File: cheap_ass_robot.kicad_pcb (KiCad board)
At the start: 2 copper layers, 68.6 x 53.3 mm, 43 parts, among them IC1 MC34063A, IC2 ATMEGA328P-AU-R, IC3 FT232RL, IC4 L293DD, J1 USB_B, J2 DIGITAL 2, J3 ANALOG IN, J4 POWER, J5 DIGITAL 1, M1 Motor_DC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

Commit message: fixed diagram level electrical issues and added caps from xtal to gnd
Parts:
- added C6: 22pF, Capacitors_SMD:C_0805, F.Cu at (148.6, 69.8)
- added C7: 22pF, Capacitors_SMD:C_0805, F.Cu at (152.4, 69.8)
- renumbered C8 to C10, C9 to C11, C10 to C12, C11 to C13, C6 to C8, C7 to C9
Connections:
- C10 pad 1: Net-(C4-Pad1) -> Net-(C10-Pad1)
- C11 pad 1: Net-(C4-Pad1) -> Net-(C10-Pad1)
- C4 pad 1: Net-(C4-Pad1) -> Net-(C10-Pad1)
- C9 pad 1: Net-(C4-Pad1) -> Net-(C10-Pad1)
- D2 pad 1: Net-(C4-Pad1) -> Net-(C10-Pad1)
- D3 pad 1: Net-(C4-Pad1) -> Net-(C10-Pad1)
- D4 pad 2: Net-(C4-Pad1) -> Net-(C10-Pad1)
- D5 pad 2: Net-(C4-Pad1) -> Net-(C10-Pad1)
- IC2 pad 18: Net-(C4-Pad1) -> Net-(C10-Pad1)
- IC2 pad 21: Net-(IC2-Pad21) -> Net-(BT1-Pad2)
- IC2 pad 23: (no net) -> Net-(IC2-Pad23)
- IC2 pad 24: (no net) -> Net-(IC2-Pad24)
- IC2 pad 25: (no net) -> Net-(IC2-Pad25)
- IC2 pad 4: Net-(C4-Pad1) -> Net-(C10-Pad1)
- IC2 pad 6: Net-(C4-Pad1) -> Net-(C10-Pad1)
- IC3 pad 20: Net-(C4-Pad1) -> Net-(C10-Pad1)
- IC3 pad 4: Net-(C4-Pad1) -> Net-(C10-Pad1)
- IC4 pad 1: Net-(C4-Pad1) -> Net-(C10-Pad1)
- IC4 pad 10: Net-(C4-Pad1) -> Net-(C10-Pad1)
- IC4 pad 11: Net-(C4-Pad1) -> Net-(C10-Pad1)
- IC4 pad 14: Net-(IC4-Pad14) -> Net-(BT1-Pad2)
- IC4 pad 18: (no net) -> Net-(IC4-Pad18)
- IC4 pad 20: Net-(C4-Pad1) -> Net-(C10-Pad1)
- J2 pad 8: Net-(J2-Pad8) -> Net-(C10-Pad1)
- J3 pad 1: Net-(IC2-Pad20) -> Net-(IC2-Pad23)
- J3 pad 2: Net-(IC2-Pad21) -> Net-(IC2-Pad24)
- J3 pad 3: Net-(IC2-Pad22) -> Net-(IC2-Pad25)
- J4 pad 1: Net-(J2-Pad8) -> Net-(C10-Pad1)
- J4 pad 4: Net-(J2-Pad8) -> Net-(C10-Pad1)
- J4 pad 7: Net-(J2-Pad8) -> Net-(C10-Pad1)
- M2 pad 2: Net-(IC4-Pad14) -> Net-(IC4-Pad18)
- R4 pad 2: Net-(C4-Pad1) -> Net-(C10-Pad1)
- R6 pad 2: Net-(C4-Pad1) -> Net-(C10-Pad1)
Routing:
- net Net-(C4-Pad1): track 191.9 -> 0.00 mm, vias 15 -> 0
- net Net-(J2-Pad8): track 97.9 -> 0.00 mm
- net Net-(C10-Pad1): track 0.00 -> 40.8 mm, vias 0 -> 19
- net Net-(IC2-Pad25): track 0.00 -> 38.6 mm
- net Net-(IC2-Pad23): track 0.00 -> 36.7 mm
- net Net-(IC2-Pad24): track 0.00 -> 36.7 mm
- net Net-(IC2-Pad22): track 35.7 -> 0.00 mm
- net Net-(IC4-Pad14): track 34.7 -> 0.00 mm, vias 1 -> 0
- net Net-(IC2-Pad21): track 34.2 -> 0.00 mm
- net Net-(C3-Pad1): track 70.3 -> 44.3 mm, vias 8 -> 2
- net Net-(IC2-Pad31): track 38.5 -> 61.1 mm
- net Net-(IC4-Pad18): track 0.00 -> 22.0 mm, vias 0 -> 1
- net Net-(C6-Pad1): track 16.1 -> 33.0 mm
- net Net-(IC2-Pad30): track 41.7 -> 57.6 mm
- net Net-(IC2-Pad16): track 49.7 -> 38.2 mm, vias 2 -> 0
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- added copper zone on B.Cu, net Net-(C10-Pad1)

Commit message: will probably be revision alpha-1
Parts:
- added REF**: MountingHole_3.2mm_M3, Mounting_Holes:MountingHole_3.2mm_M3, F.Cu at (130.7, 63.1)
- added REF**: MountingHole_3.2mm_M3, Mounting_Holes:MountingHole_3.2mm_M3, F.Cu at (181.5, 78.4)
- added REF**: MountingHole_3.2mm_M3, Mounting_Holes:MountingHole_3.2mm_M3, F.Cu at (181.5, 106.3)
- added REF**: MountingHole_3.2mm_M3, Mounting_Holes:MountingHole_3.2mm_M3, F.Cu at (129.4, 111.3)
- C4: footprint Capacitors_SMD:CP_Elec_4x5.7 -> Capacitors_SMD:CP_Elec_6.3x7.7
- D2, D3: footprint Diodes_SMD:D_SMB -> Diodes_SMD:D_SOD-123F
- L1: footprint Inductors_SMD:L_1210 -> Inductors_SMD:L_0805
- moved C5 2.84 mm to (129.5, 85.1), turned to 180 degrees
- moved C7 2.54 mm to (154.9, 69.8), turned to 0 degrees
- moved C13 1.80 mm to (137.2, 85.1), turned to 180 degrees
- moved C6 1.27 mm to (149.9, 69.8), turned to 0 degrees
- moved D2 1.27 mm to (137.2, 106.7)
- moved C11 1.27 mm to (119.4, 63.5), turned to 180 degrees
- moved C9 1.27 mm to (124.5, 63.5), turned to 0 degrees
- moved C8 1.08 mm to (167.6, 88.9), turned to 180 degrees
- turned C12 to 0 degrees
- turned C2 to 180 degrees
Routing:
- net Net-(BT1-Pad2): track 61.6 -> 58.3 mm
- net Net-(C3-Pad1): track 44.3 -> 41.3 mm
- net Net-(C8-Pad1): track 13.3 -> 10.7 mm
- net Net-(C10-Pad1): track 40.8 -> 38.8 mm, vias 19 -> 18
- net Net-(C13-Pad2): track 54.0 -> 56.0 mm
- net Net-(C7-Pad1): track 18.8 -> 20.5 mm
- net Net-(C2-Pad2): track 38.0 -> 39.5 mm
- net Net-(IC2-Pad28): track 100.5 -> 99.3 mm
- net Net-(IC2-Pad26): track 42.9 -> 41.9 mm
- net Net-(D2-Pad2): track 22.2 -> 23.2 mm
- net Net-(C6-Pad1): track 33.0 -> 33.9 mm
- net Net-(IC2-Pad27): track 98.2 -> 97.4 mm
- net Net-(IC1-Pad7): track 27.7 -> 28.3 mm
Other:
- board text added: "Griffith Cybernetics Cheap Ass Robot Rev. Alpha-1 2018-09-27"

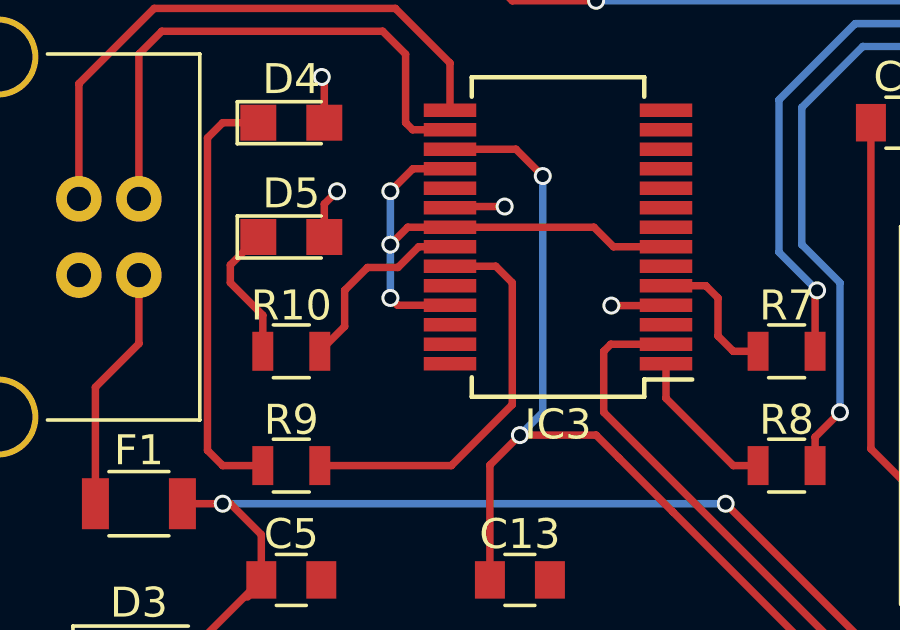
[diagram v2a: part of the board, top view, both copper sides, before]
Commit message: sync; most recent change was fixing missed connection to ground on ftdi chip
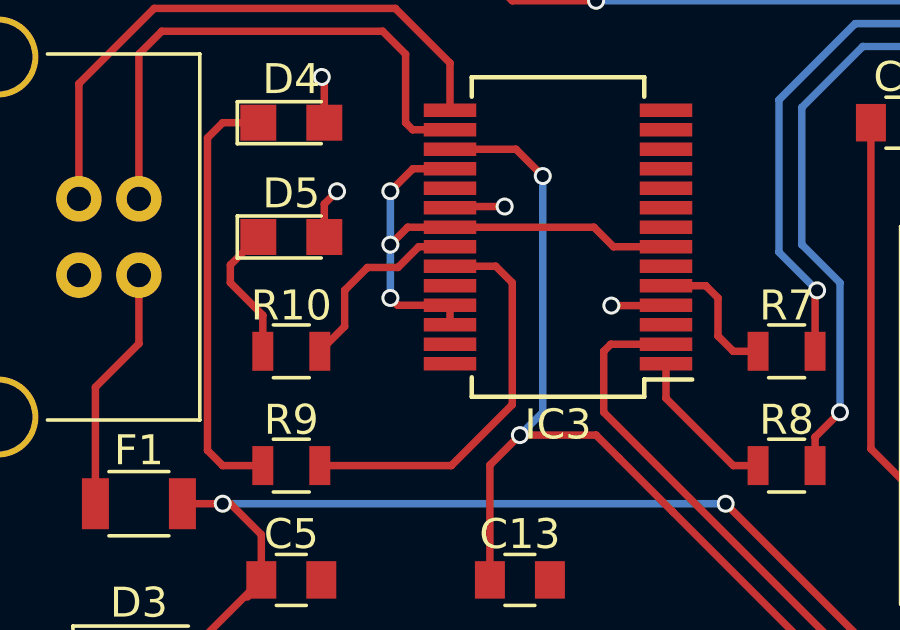
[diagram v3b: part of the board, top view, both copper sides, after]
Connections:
- IC3 pad 26: Net-(IC3-Pad26) -> Net-(BT1-Pad2)
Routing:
- net Net-(BT1-Pad2): track 58.3 -> 59.0 mm

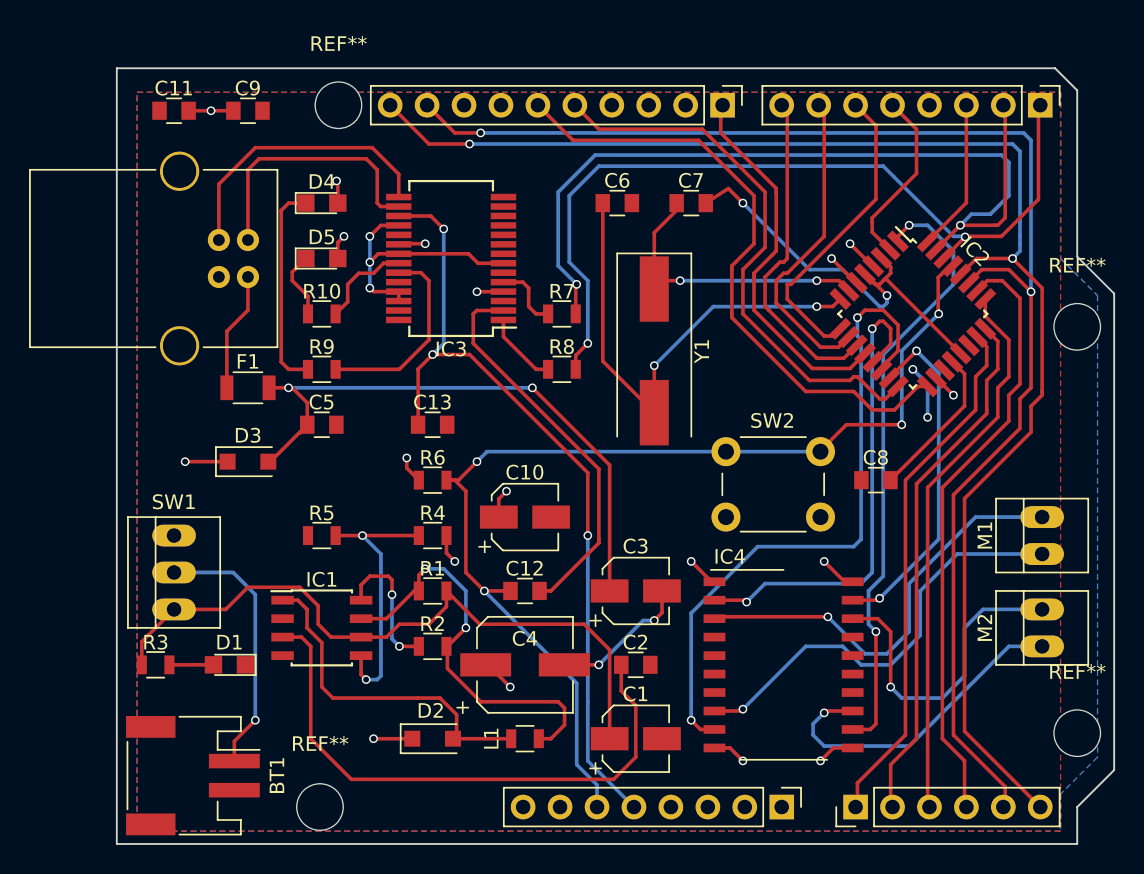
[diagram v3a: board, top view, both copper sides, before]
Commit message: widen traces on on segments likely to pull larger currents
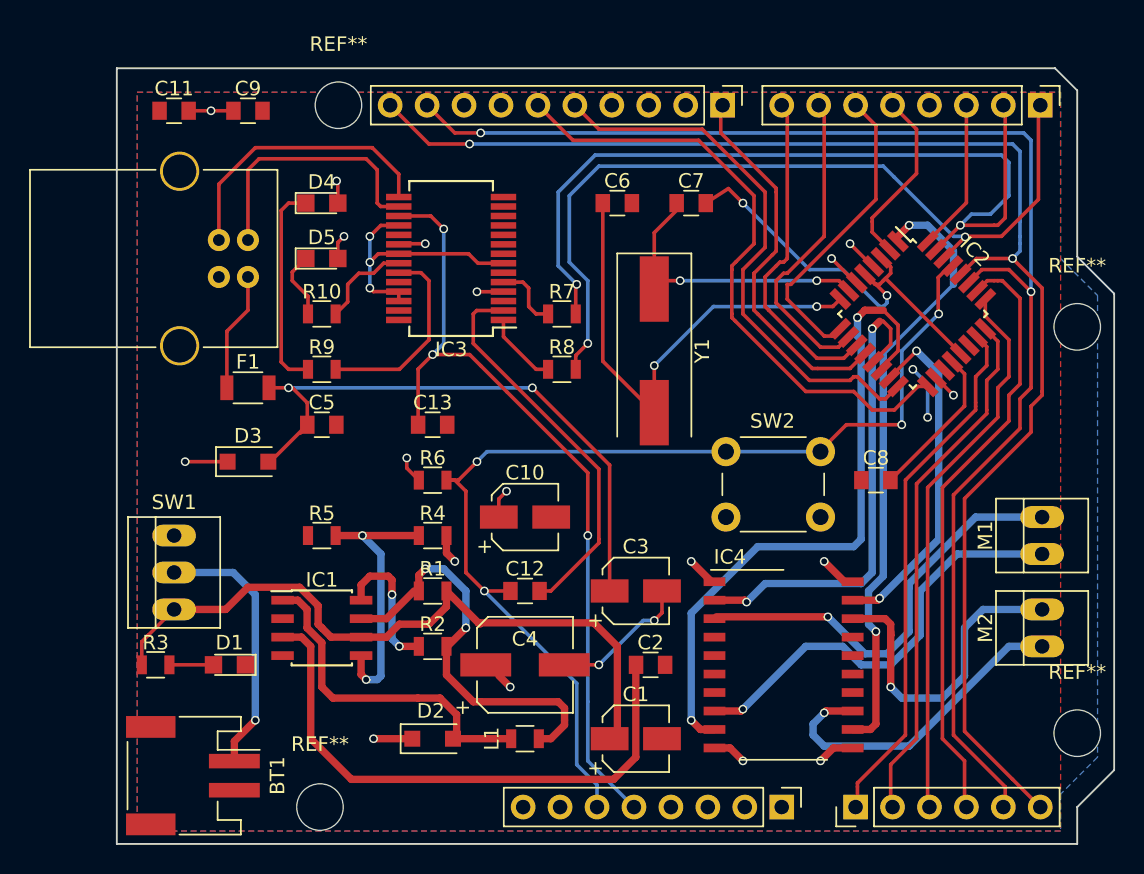
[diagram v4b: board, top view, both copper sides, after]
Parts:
- moved C2 1.02 mm to (152.1, 101.6)
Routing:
- net Net-(C1-Pad1): track 47.2 -> 48.2 mm
- net Net-(IC4-Pad18): track 22.0 -> 22.5 mm
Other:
- board text added: "Griffith Cybernetics Cheap Ass Robot Rev. Alpha-2 2019-04-15"
- board text removed: "Griffith Cybernetics Cheap Ass Robot Rev. Alpha-1 2018-09-27"
